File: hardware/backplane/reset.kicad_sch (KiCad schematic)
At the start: 17 parts, among them SW1 Reset, U7 74VHCV07FT

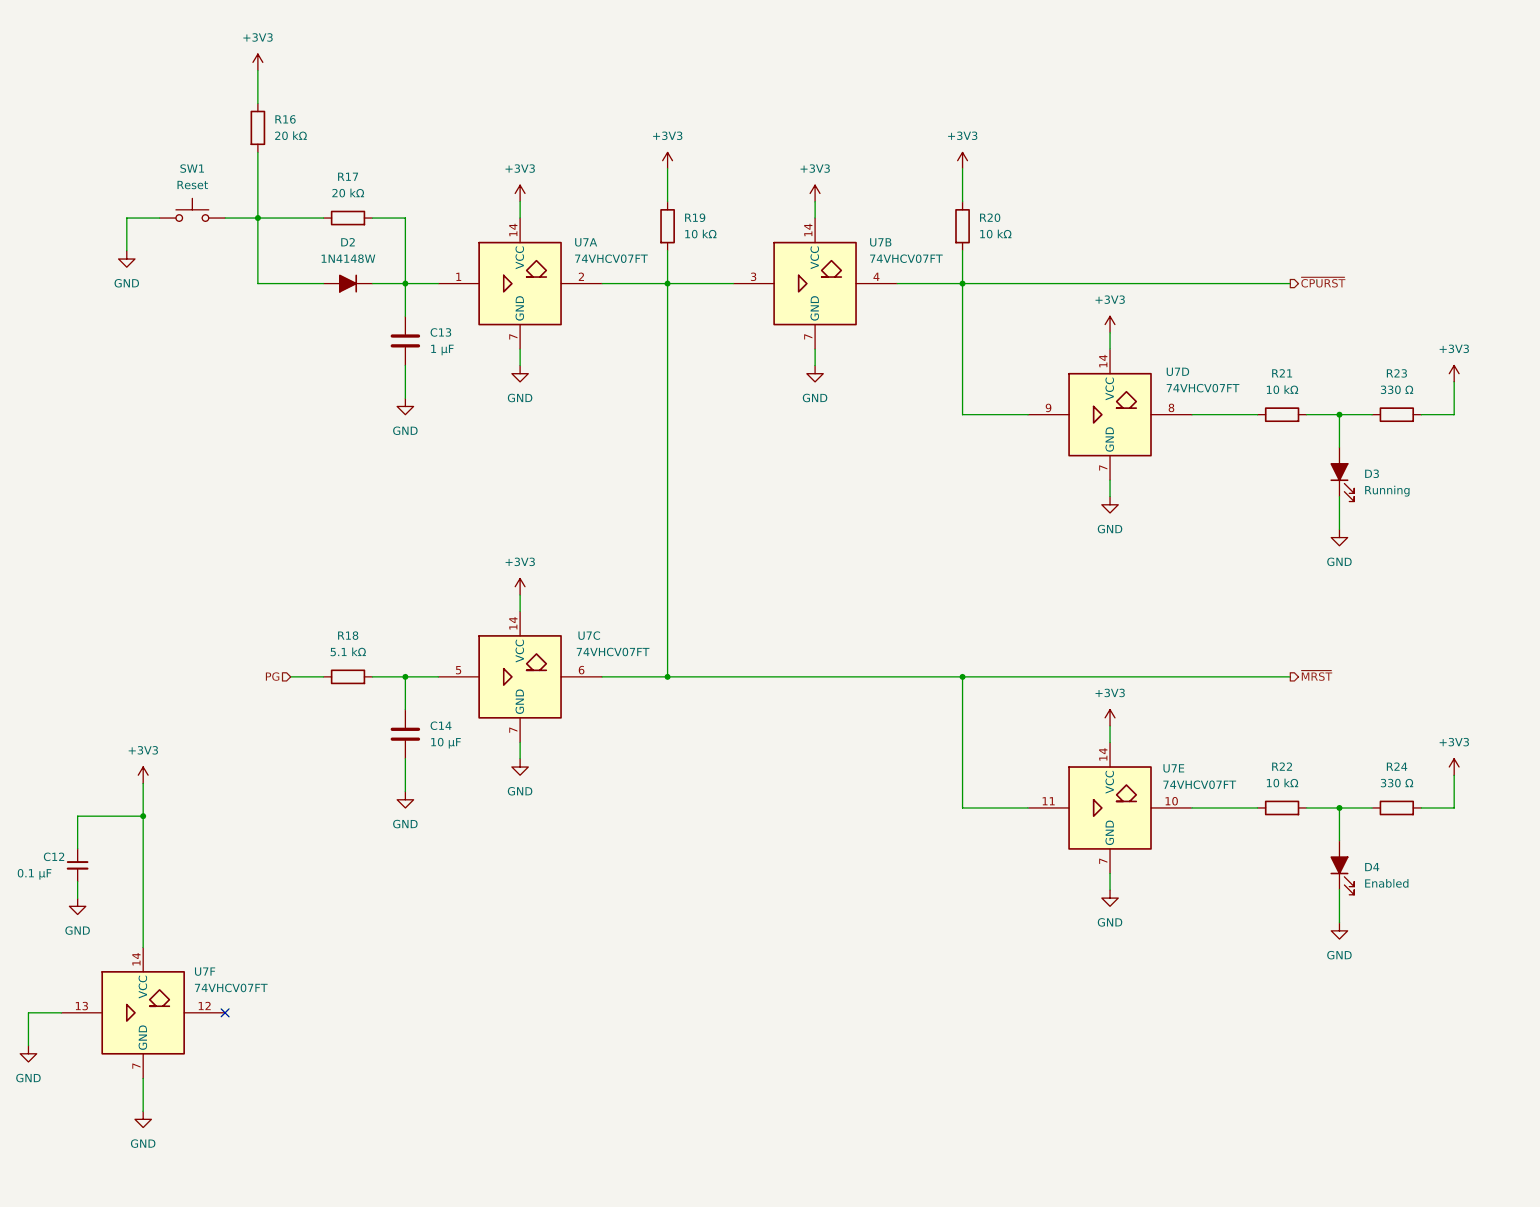
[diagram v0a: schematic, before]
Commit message: feat: Re-add peripheral MCLK, add to memory lines (#3)
Need MCLK to maintain peripheral synchronization.  Add missing memory
access size and latch lines.
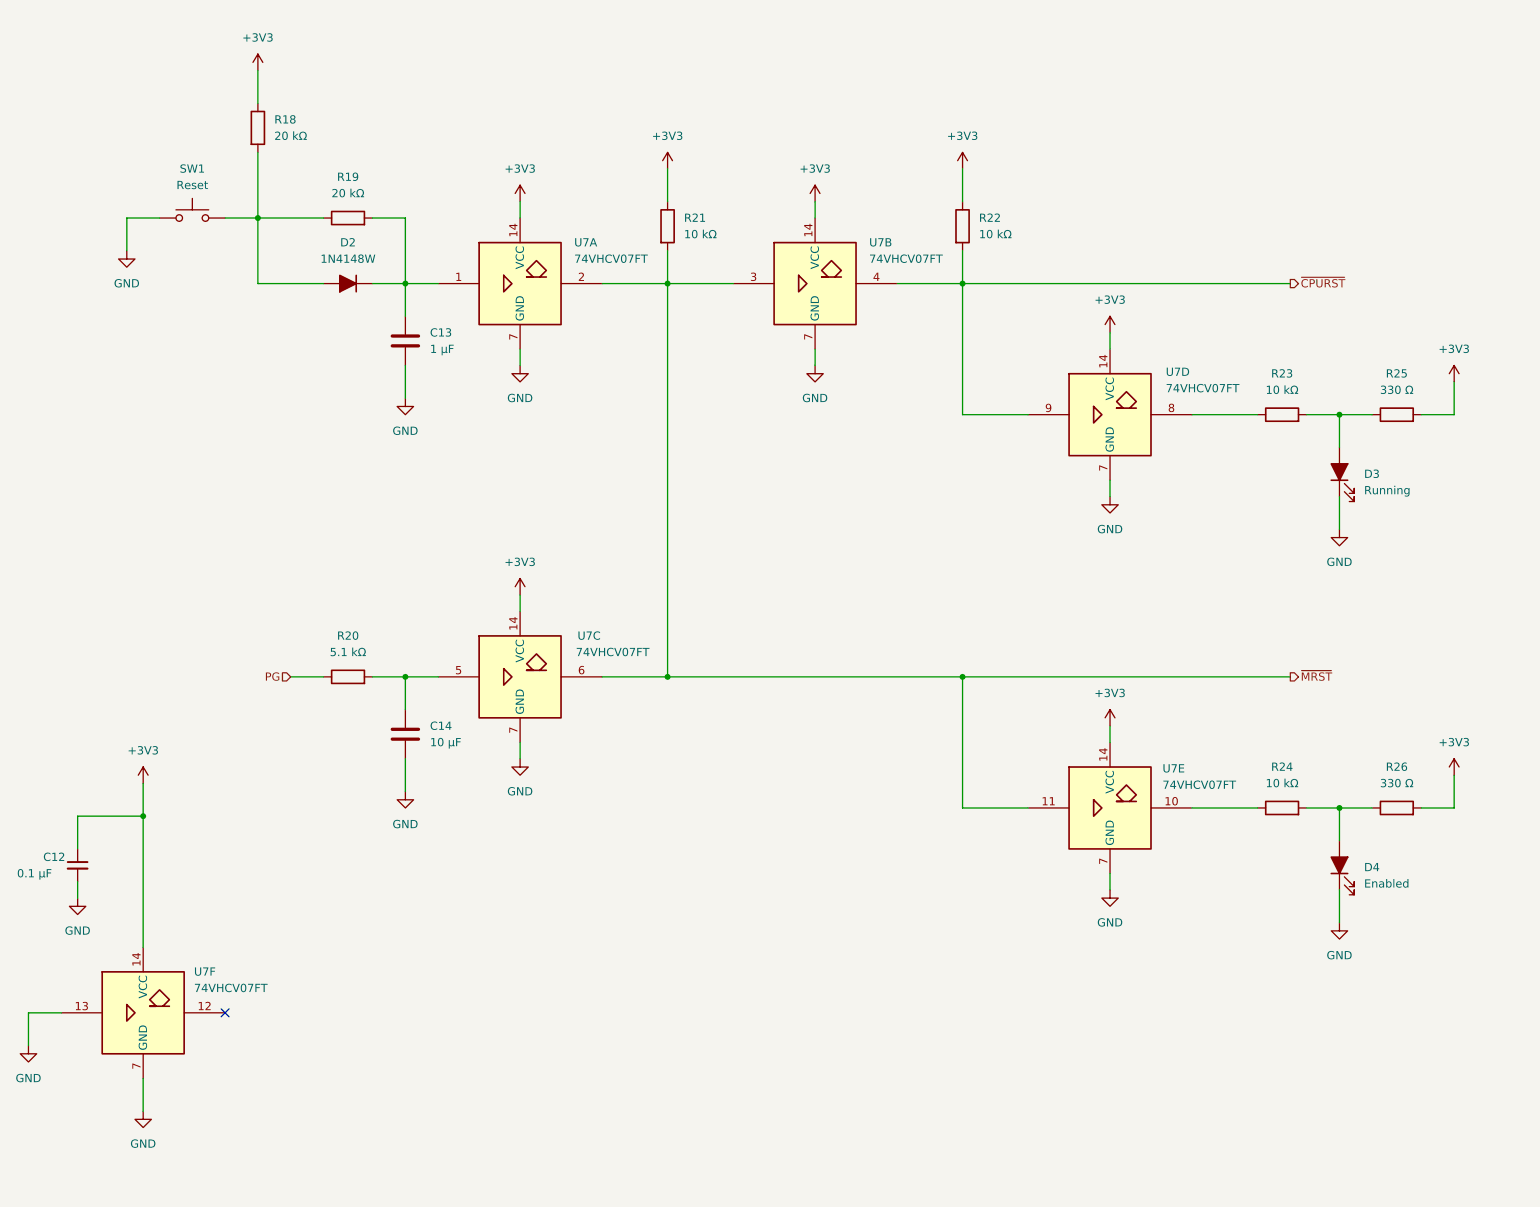
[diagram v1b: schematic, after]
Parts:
- renumbered R16 to R18, R17 to R19, R18 to R20, R19 to R21, R20 to R22, R21 to R23, R22 to R24, R23 to R25, R24 to R26

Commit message: feat: Assign footprints, add testpoints
 * Verify all footprints are assigned.
 * Create testpoints for key signals.
 * Reorganize component libraries.
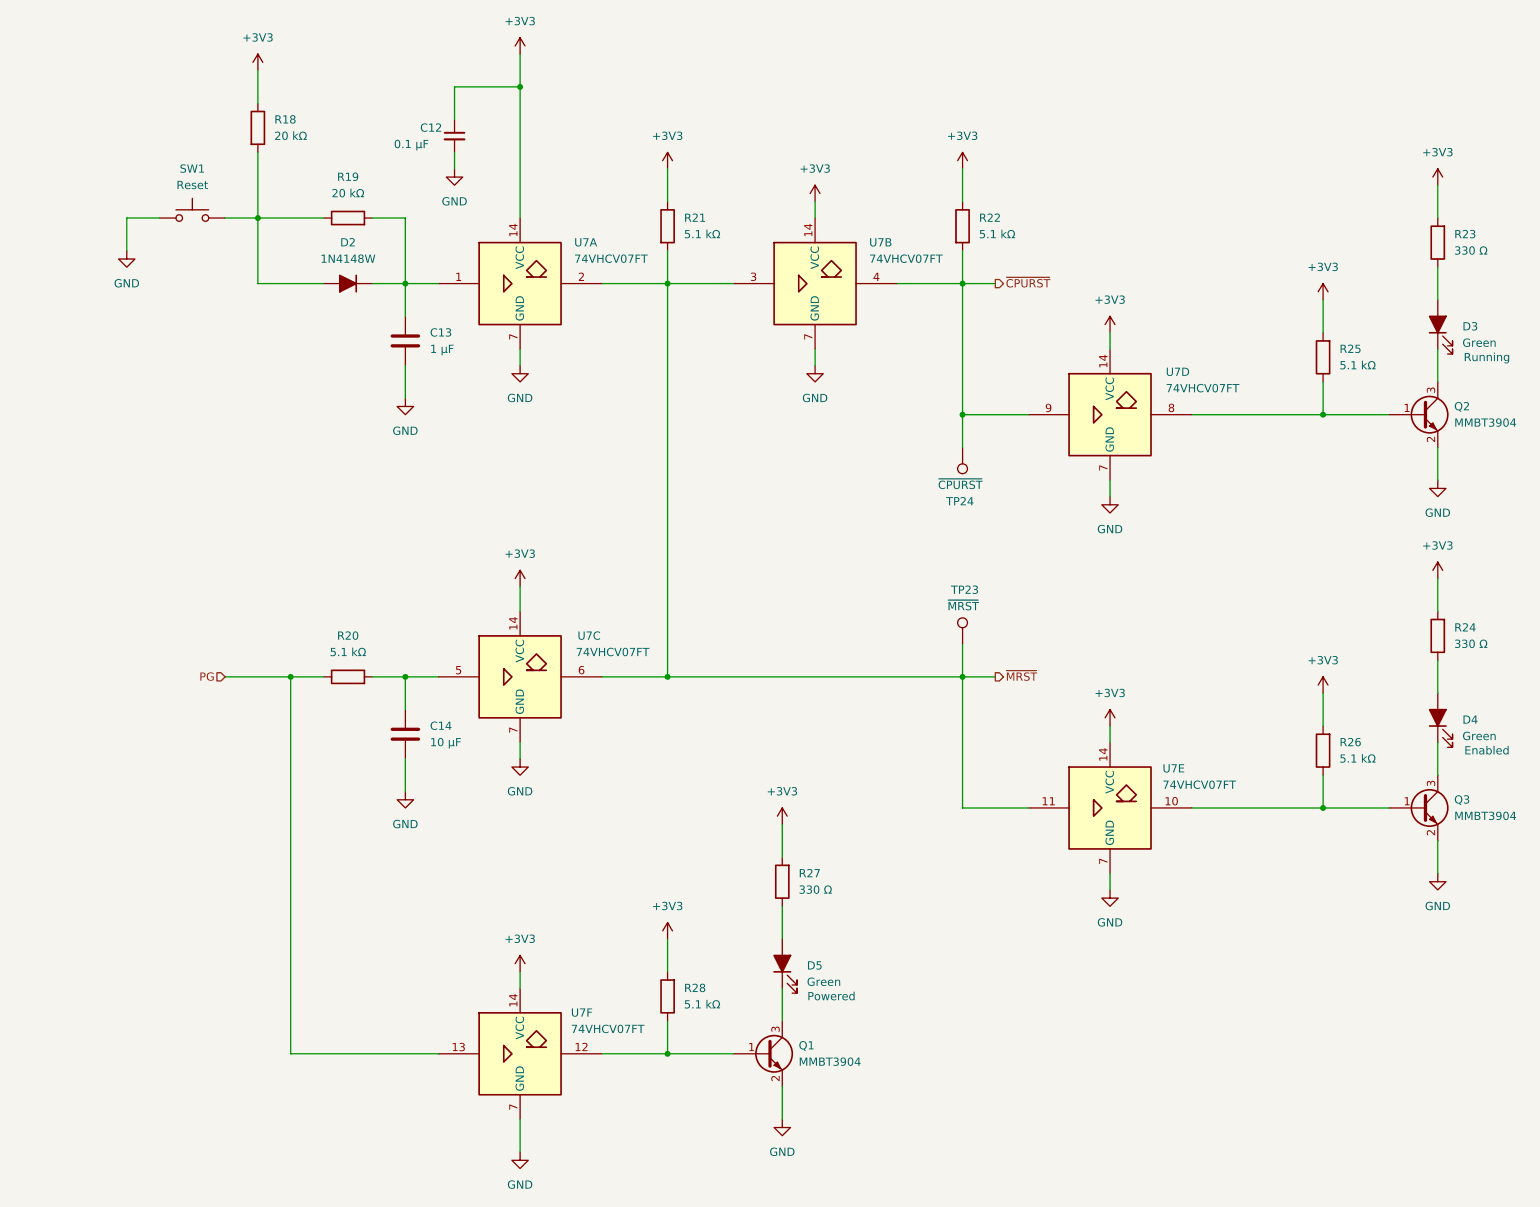
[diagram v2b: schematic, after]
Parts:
- added D5: Green, LED_SMD:LED_0603_1608Metric, symbol Device:LED_Filled
- added Q1, Q2, Q3: MMBT3904, Package_TO_SOT_SMD:SOT-23, symbol Transistor_BJT:MMBT3904
- added R27: 330 Ω, Resistor_SMD:R_0402_1005Metric, symbol Device:R
- added R28: 5.1 kΩ, Resistor_SMD:R_0402_1005Metric, symbol Device:R
- added TP23: ~{MRST}, TestPoint:TestPoint_Pad_D1.0mm, symbol Connector:TestPoint
- added TP24: ~{CPURST}, TestPoint:TestPoint_Pad_D1.0mm, symbol Connector:TestPoint
- C12: footprint (none) -> Capacitor_SMD:C_0402_1005Metric; Part Number (none) -> GRM155R71C104KA88J
- C13: footprint (none) -> Capacitor_SMD:C_0603_1608Metric; Part Number (none) -> CC0603KRX7R7BB105
- C14: footprint (none) -> Capacitor_SMD:C_0805_2012Metric; Part Number (none) -> GRM21BR71A106KA73L
- D2: footprint (none) -> Diode_SMD:D_SOD-123F; Part Number (none) -> 1N4148W
- D3: value Running -> Green; footprint (none) -> LED_SMD:LED_0603_1608Metric; Indicates (none) -> Running; Part Number (none) -> 150060VS55040
- D4: value Enabled -> Green; footprint (none) -> LED_SMD:LED_0603_1608Metric; Indicates (none) -> Enabled; Part Number (none) -> 150060VS55040
- R18, R19: footprint (none) -> Resistor_SMD:R_0402_1005Metric; Part Number (none) -> RC0402FR-0720KL
- R20: footprint (none) -> Resistor_SMD:R_0402_1005Metric; Part Number (none) -> CR0402-FX-5101GLF
- R21, R22: value 10 kΩ -> 5.1 kΩ; footprint (none) -> Resistor_SMD:R_0402_1005Metric; Part Number (none) -> CR0402-FX-5101GLF
- R23, R24: value 10 kΩ -> 330 Ω; footprint (none) -> Resistor_SMD:R_0402_1005Metric; Part Number (none) -> RC0402FR-07330RL
- R25, R26: value 330 Ω -> 5.1 kΩ; footprint (none) -> Resistor_SMD:R_0402_1005Metric; Part Number (none) -> CR0402-FX-5101GLF
- SW1: footprint (none) -> Button_Switch_SMD:SW_SPST_TL3305B; Part Number (none) -> TL3305BF260QG
- U7: footprint (none) -> Package_SO:TSSOP-14_4.4x5mm_P0.65mm; Part Number (none) -> 74VHCV07FT
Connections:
- net +3V3: now also R23.2, R24.2, R27.2, R28.2
- net GND: now also Q1.2 (E), Q2.2 (E), Q3.2 (E); no longer D3.1 (K), D4.1 (K), U7.13
- net PG: now also U7.13
- net ~{CPURST}: now also TP24.1
- net ~{MRST}: now also TP23.1
- net at U7.10: now also R26.1, Q3.1 (B); no longer R24.1
- net at U7.8: now also R25.1, Q2.1 (B); no longer R23.1
- net at U7.12: now also Q1.1 (B), R28.1
- new net: D5.2 (A), R27.1
- new net: D5.1 (K), Q1.3 (C)
- new net: D4.1 (K), Q3.3 (C)
- new net: D3.1 (K), Q2.3 (C)
- new net: D4.2 (A), R24.1
- new net: D3.2 (A), R23.1
- no-connect marks 1 -> 0
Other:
- moved on the sheet: C12, U7F

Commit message: feat: Apply bus arch changes to backplane schematic
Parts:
- TP24: value ~{CPURST} -> ~{CRST}
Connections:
- net ~{CPURST} renamed ~{CRST}
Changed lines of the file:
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@@
 		)
 	)
-	(hierarchical_label "~{CPURST}"
+	(hierarchical_label "~{CRST}"
 		(shape output)
 		(at 172.72 55.88 0)
@@
 			)
 		)
-		(property "Value" "~{CPURST}"
-			(at 163.83 87.122 0)
-			(effects
-				(font
+		(property "Value" "~{CRST}"
+			(at 165.1 87.122 0)
+			(effects
+				(font
